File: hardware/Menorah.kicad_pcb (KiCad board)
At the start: 2 copper layers, 111.8 x 130.3 mm, 0 parts

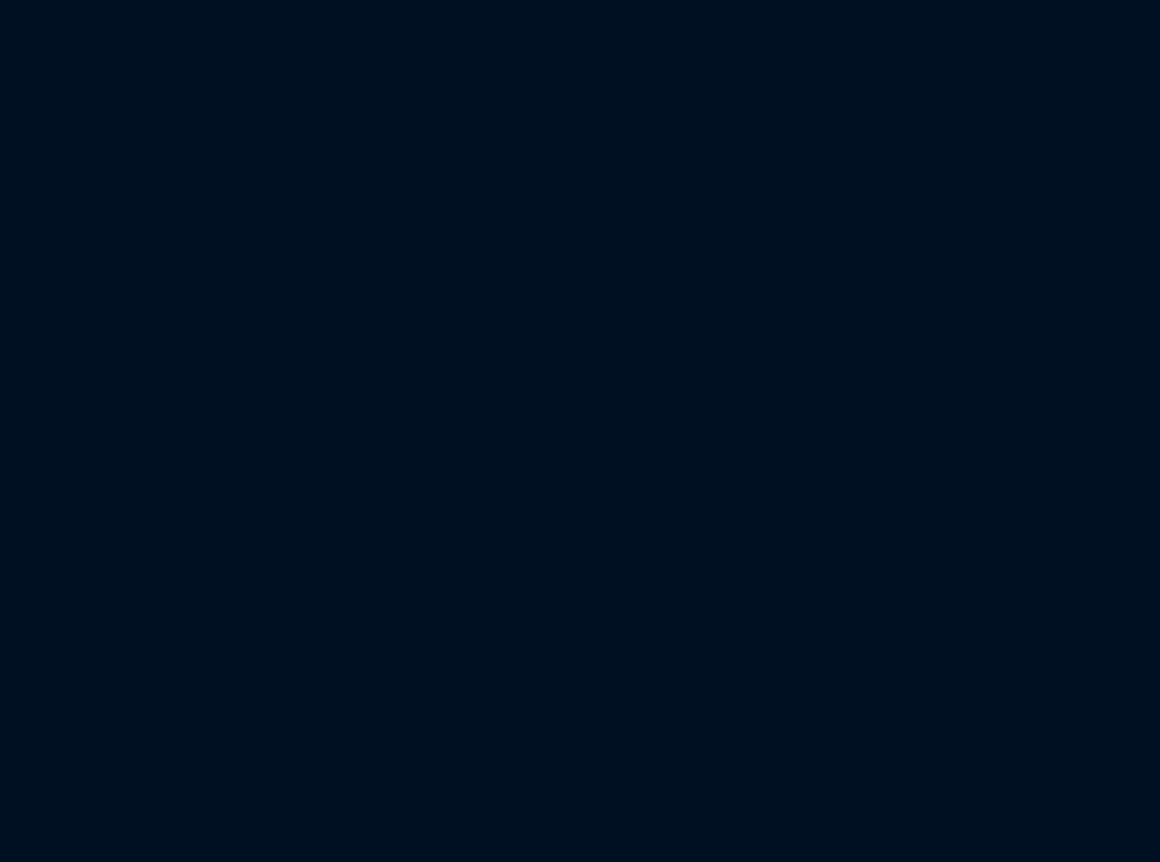
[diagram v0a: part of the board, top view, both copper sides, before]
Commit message: assigned footprints, started layout
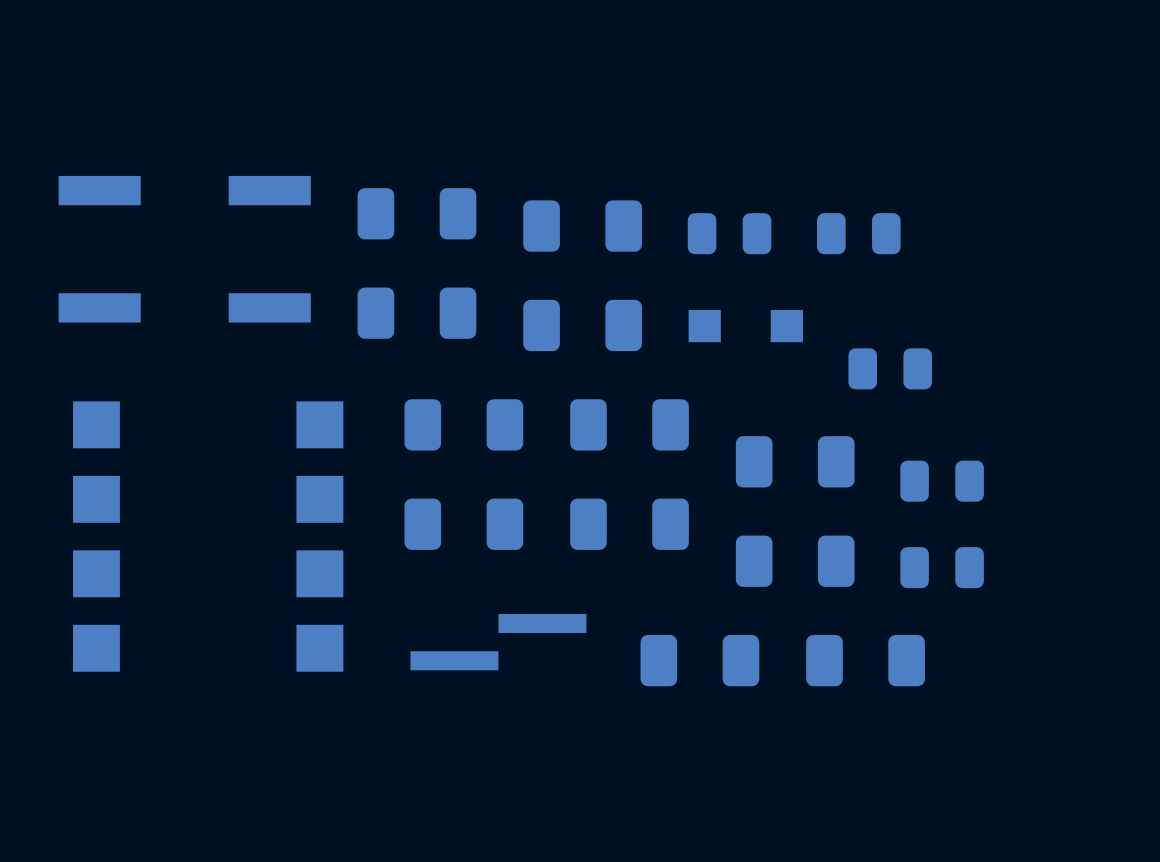
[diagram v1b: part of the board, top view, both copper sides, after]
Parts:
- added BT1: Battery, Connector_PinHeader_1.27mm:PinHeader_1x02_P1.27mm_Vertical_SMD_Pin1Left, B.Cu at (63.5, 157.5)
- added D1: LED, LED_SMD:LED_1206_3216Metric, B.Cu at (62.3, 153.5)
- added D10: LED, LED_SMD:LED_1206_3216Metric, B.Cu at (60.7, 146.3)
- added D11: LED, LED_SMD:LED_1206_3216Metric, B.Cu at (66.4, 143.3)
- added D12: LED, LED_SMD:LED_1206_3216Metric, B.Cu at (73.6, 151.3)
- added D13: 1N4004, Diode_SMD:D_SOD-123F, B.Cu at (71.9, 146.7)
- added D2: LED, LED_SMD:LED_1206_3216Metric, B.Cu at (62.3, 150.1)
- added D3: LED, LED_SMD:LED_1206_3216Metric, B.Cu at (70.4, 158.1)
- added D4: LED, LED_SMD:LED_1206_3216Metric, B.Cu at (68.0, 153.5)
- added D5: LED, LED_SMD:LED_1206_3216Metric, B.Cu at (60.7, 142.9)
- added D6: LED, LED_SMD:LED_1206_3216Metric, B.Cu at (66.4, 146.7)
- added D7: LED, LED_SMD:LED_1206_3216Metric, B.Cu at (68.0, 150.1)
- added D8: LED, LED_SMD:LED_1206_3216Metric, B.Cu at (76.0, 158.1)
- added D9: LED, LED_SMD:LED_1206_3216Metric, B.Cu at (73.6, 154.7)
- added R1: 68, Resistor_SMD:R_0805_2012Metric, B.Cu at (78.6, 154.9)
- added R2: 68, Resistor_SMD:R_0805_2012Metric, B.Cu at (71.4, 143.6)
- added R3: 68, Resistor_SMD:R_0805_2012Metric, B.Cu at (78.6, 152.0)
- added R4: 68, Resistor_SMD:R_0805_2012Metric, B.Cu at (76.9, 148.2)
- added R5: 4k7, Resistor_SMD:R_0805_2012Metric, B.Cu at (75.8, 143.6)
- added SW1: SW_Push, Button_Switch_SMD:SW_Push_1P1T_NO_CK_KSC6xxJ, B.Cu at (52.8, 144.1)
- added U1: ATtiny85-20PU, Package_DIP:DIP-8_W7.62mm_SMDSocket_SmallPads, B.Cu at (53.6, 153.9)
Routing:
- added copper zone on F.Cu, net GND
- removed copper zone on F.Cu, net (none)

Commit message: placement progress
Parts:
- SW1: moved to F.Cu
- moved D1 145.8 mm to (112.2, 16.4)
- moved D12 145.8 mm to (123.5, 14.3)
- moved D3 145.8 mm to (120.3, 21.1)
- moved D4 145.8 mm to (117.9, 16.4)
- moved D6 145.8 mm to (116.3, 9.65)
- moved D11 145.8 mm to (116.3, 6.26)
- moved D2 145.8 mm to (112.2, 13.0)
- moved D7 145.8 mm to (117.9, 13.0)
- moved D9 145.8 mm to (123.5, 17.7)
- moved D8 143.7 mm to (128.7, 24.4)
- moved D10 116.3 mm to (106.0, 39.1)
- moved D5 109.5 mm to (93.0, 38.2)
- moved U1 98.9 mm to (144.3, 114.4)
- moved SW1 91.5 mm to (144.0, 151.3)
- moved BT1 86.2 mm to (144.1, 127.0)
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
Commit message: lotsa stuff
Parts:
- added G***: LOGO, menorah:menorah_mask, F.Cu at (142.0, 103.9)
- added G***: LOGO, menorah:menorah_traces, F.Cu at (141.4, 83.9)
- added J1: Conn_02x03_Odd_Even, Connector_PinHeader_2.54mm:PinHeader_2x03_P2.54mm_Vertical_SMD, F.Cu at (136.3, 132.3)
- BT1, D1, D13, D2, D3, D4, D5, D6, D7, D8, D9, R1, R2, R3, R4, R5, U1: moved to F.Cu
- D10, D11, D12: value LED -> 1N4004; footprint LED_SMD:LED_1206_3216Metric -> Diode_SMD:D_SOD-123F; moved to F.Cu
- SW1: moved to B.Cu
- moved D11 81.1 mm to (145.1, 82.1), turned to 180 degrees
- moved D9 70.7 mm to (192.8, 31.7)
- moved D12 68.8 mm to (145.1, 79.6)
- moved D7 53.1 mm to (167.5, 32.1)
- moved D8 52.1 mm to (180.1, 32.6)
- moved D5 50.0 mm to (141.9, 28.2)
- moved D10 49.1 mm to (144.0, 70.3), turned to 180 degrees
- moved D6 45.0 mm to (154.6, 33.3)
- moved R2 32.3 mm to (140.6, 101.7), turned to 270 degrees
- moved R4 29.3 mm to (147.1, 100.8), turned to 270 degrees
- moved R3 26.9 mm to (143.9, 100.8), turned to 270 degrees
- moved D1 26.5 mm to (91.2, 32.6)
- moved R1 24.0 mm to (137.1, 100.8), turned to 270 degrees
- moved U1 22.3 mm to (161.5, 128.5)
- moved D2 21.8 mm to (103.9, 33.2)
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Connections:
- net Net-(D13-Pad2) renamed VCC
- net Net-(R1-Pad2) renamed MISO
- net Net-(R2-Pad2) renamed SCK
- net Net-(R5-Pad1) renamed MOSI
- D10 pad 2: Net-(D1-Pad2) -> Net-(D1-Pad1)
- D11 pad 1: Net-(D1-Pad1) -> Net-(D1-Pad2)
- D12 pad 1: Net-(D1-Pad2) -> Net-(D10-Pad1)
- D12 pad 2: Net-(D10-Pad1) -> Net-(D1-Pad2)
- D6 pad 2: Net-(D1-Pad2) -> Net-(D10-Pad1)
- D7 pad 2: Net-(D10-Pad1) -> Net-(D1-Pad2)
- U1 pad 1: Net-(U1-Pad1) -> RST
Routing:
- net Net-(D3-Pad1): track 0.00 -> 195.2 mm
- net Net-(D1-Pad1): track 0.00 -> 188.0 mm
- net Net-(D1-Pad2): track 0.00 -> 150.7 mm
- net Net-(D10-Pad1): track 0.00 -> 149.0 mm
- added copper zone on B.Cu, net GND
- removed copper zone on F.Cu, net GND
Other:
- board size 111.8 x 130.3 mm -> 111.6 x 130.3 mm

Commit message: layout progress
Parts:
- added REF**: R_0805_2012Metric, Resistor_SMD:R_0805_2012Metric, F.Cu at (141.4, 86.0)
- added REF**: R_0805_2012Metric, Resistor_SMD:R_0805_2012Metric, F.Cu at (145.5, 89.4)
- added REF**: R_0805_2012Metric, Resistor_SMD:R_0805_2012Metric, F.Cu at (139.0, 88.4)
- added REF**: R_0805_2012Metric, Resistor_SMD:R_0805_2012Metric, F.Cu at (137.9, 77.0)
- added REF**: R_0805_2012Metric, Resistor_SMD:R_0805_2012Metric, F.Cu at (145.5, 77.2)
- added REF**: R_0805_2012Metric, Resistor_SMD:R_0805_2012Metric, F.Cu at (139.7, 70.3)
- added REF**: R_0805_2012Metric, Resistor_SMD:R_0805_2012Metric, F.Cu at (144.2, 66.4)
- added REF**: R_0805_2012Metric, Resistor_SMD:R_0805_2012Metric, F.Cu at (145.5, 85.1)
- moved U1 26.3 mm to (142.1, 110.7), turned to 180 degrees
- moved R5 20.8 mm to (139.2, 119.9), turned to 180 degrees
- moved BT1 18.9 mm to (145.2, 118.2), turned to 0 degrees
- moved D13 16.9 mm to (139.7, 117.6)
- moved J1 8.88 mm to (142.1, 125.6), turned to 90 degrees
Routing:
- net Net-(D3-Pad1): track 195.2 -> 252.3 mm
- net MOSI: track 0.00 -> 44.9 mm, vias 0 -> 2
- net SCK: track 0.00 -> 33.9 mm
- net MISO: track 0.00 -> 30.4 mm
- net Net-(D1-Pad1): track 188.0 -> 214.1 mm
- net RST: track 0.00 -> 16.5 mm
- net Net-(R3-Pad2): track 0.00 -> 11.1 mm
- net Net-(D1-Pad2): track 150.7 -> 160.3 mm
- net Net-(R4-Pad2): track 0.00 -> 9.15 mm
- net VCC: track 0.00 -> 9.07 mm
- net Net-(BT1-Pad1): track 0.00 -> 2.64 mm
- net GND: vias 0 -> 27
- added copper zone on F.Cu, net GND
